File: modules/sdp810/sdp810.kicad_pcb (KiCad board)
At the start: 4 copper layers, 24 x 20 mm, 5 parts, among them J1 SFP+, U1 XGZP6899D

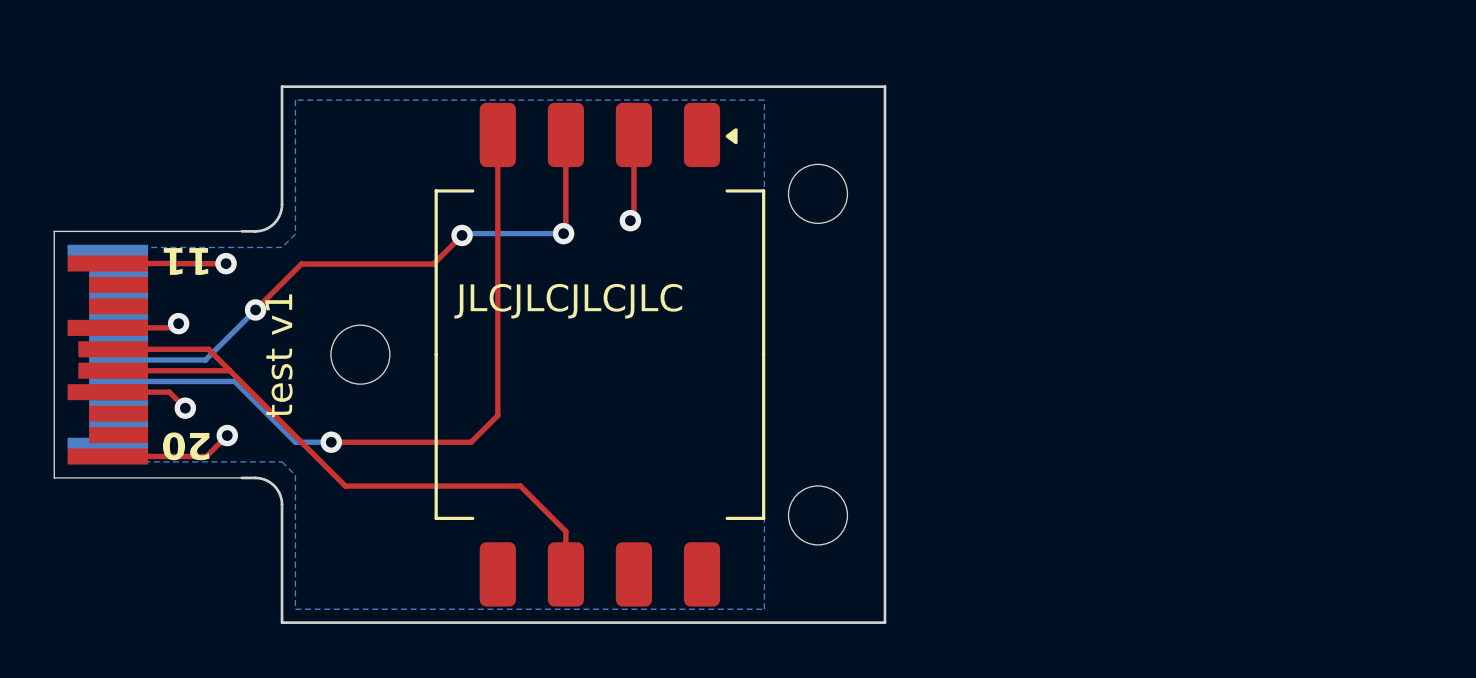
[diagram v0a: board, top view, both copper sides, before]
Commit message: SDP810 module PCB (L42) and module length scheme
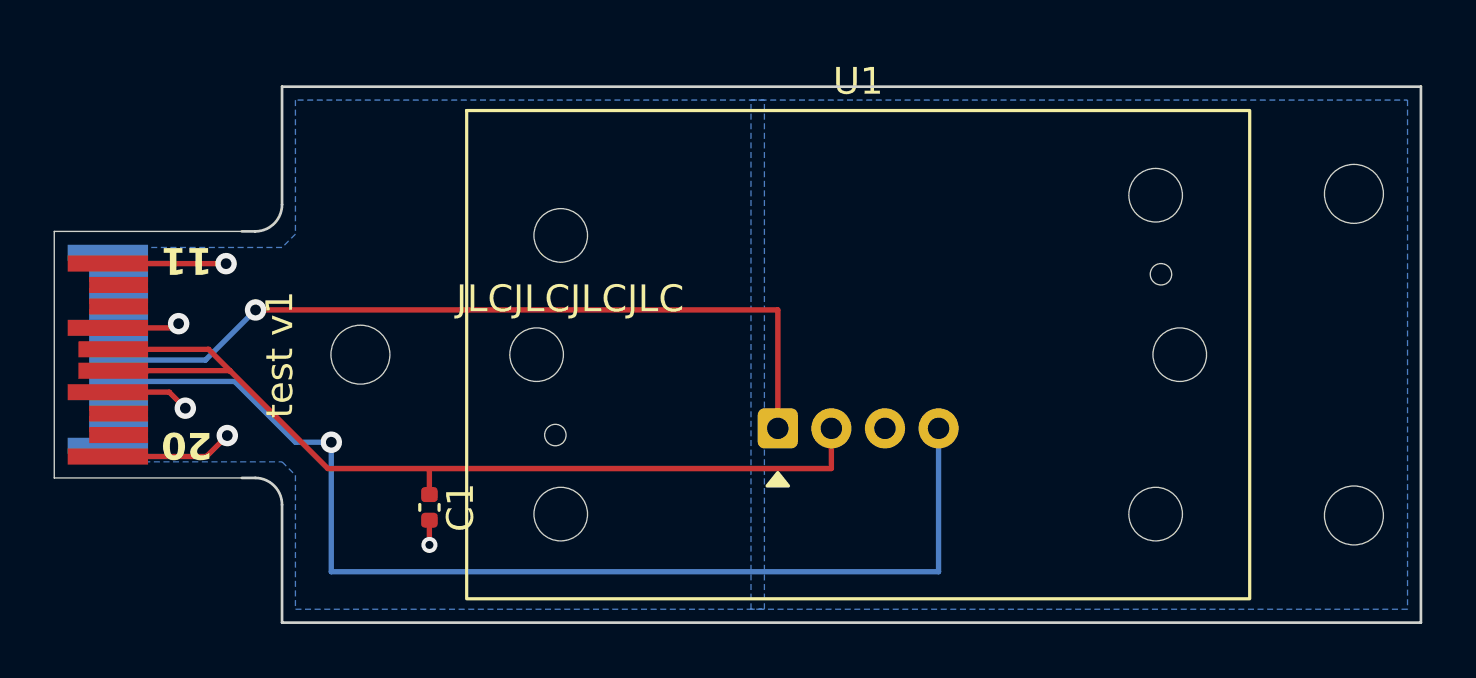
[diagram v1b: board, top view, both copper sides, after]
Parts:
- added C1: 100nF, Capacitor_SMD:C_0402_1005Metric, F.Cu at (92.0, 81.9)
- U1: value XGZP6899D -> SDP810; footprint Sensor_Pressure:CFSensor_XGZP6899x -> sdp810:SDP810
- moved H1 20.0 mm to (126.5, 70.2)
- moved H3 20.0 mm to (126.5, 82.2)
- moved U1 9.64 mm to (108.0, 76.2), turned to 0 degrees
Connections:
- U1 pad 1: unconnected-(U1-NC-Pad1) -> SCL
- U1 pad 2: GND -> VDD
- U1 pad 3: SCL -> GND
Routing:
- net SDA: track 26.0 -> 41.7 mm
- net VDD: track 25.7 -> 35.5 mm
- net SCL: track 22.3 -> 29.8 mm, vias 3 -> 1
- net GND: track 18.3 -> 16.0 mm
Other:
- board size 24 x 20 mm -> 44 x 20 mm

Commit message: Hybrid sensor module, SDP810 screw mounts (interface-v3), main board J6 adoption
Hybrid module (modules/hybrid): one L42 board that takes either an SDP810 (U1)
or an XGZP6899D (U2) on a shared site at 22 mm; fit one, never both. The SDP810
is screwed down through its body bores (M2x14, Ø2.2 NPTH) into carrier nuts at
10 and 34 mm, with B-side keepouts there. J2 is a bottom-side 1x5 pogo test pad
row, GND-SCL-3V3-SDA-GND, so a reversed jig only swaps SDA/SCL. Corners R1.

Interface v3: carrier nuts at 2.925, 10, 34 and 40 mm; the 30 mm nut is gone
(it overlaps 34 mm), which retires L32 and the xgzp6899 module. New shared
footprint sensor_module:TestPads_1x05_P2.54mm. Skeleton keepouts moved to 10/34.

Main board: J6 wired up, H7 moved to 34 mm and H9 added at 10 mm, R13 5k1
pull-up on GPIO4 (shared ~SPI_CS / UART_P2C).

Removed the breakout carrier; module CI now only scans modules/ and skips
the skeleton template.
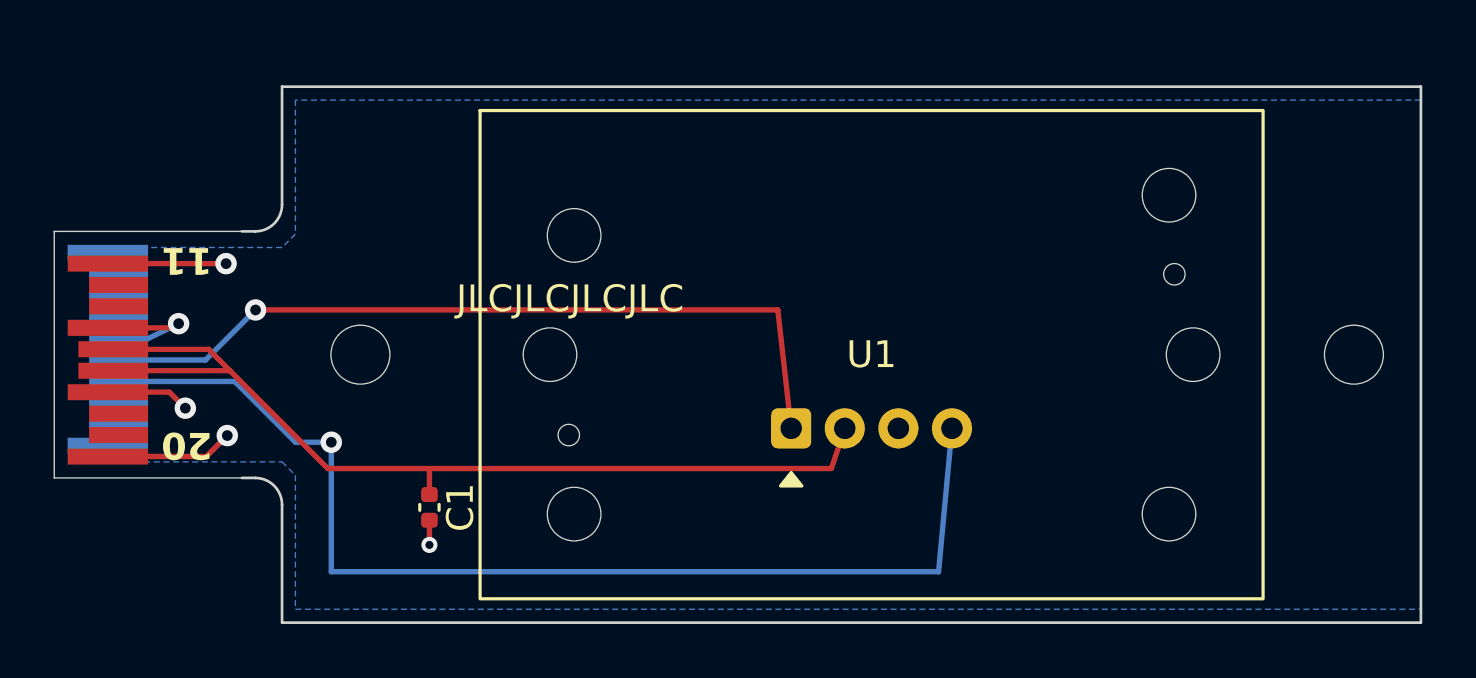
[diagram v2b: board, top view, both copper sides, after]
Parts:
- removed H3: SMSI-M2_H4mm_9774040243, MountingHole:MountingHole_2.2mm_M2
- J1: value SFP+ -> SensorModule
- moved H1 6.00 mm to (126.5, 76.2)
- moved U1 0.50 mm to (108.5, 76.2)
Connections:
- net VDD renamed +3V3
- J1 pad 6: unconnected-(J1-MOD_ABS-Pad6) -> GND
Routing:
- net GND: track 16.0 -> 18.3 mm
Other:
- copper layers 4 -> 2
- board text removed: "test v1"
